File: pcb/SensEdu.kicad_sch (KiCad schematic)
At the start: 26 parts, among them J1 Power, J10 Barrel_Jack_Switch, J13 Conn_02x01, J14 Conn_02x01, J15 Conn_02x01, J2 PWM, J3 Analog, J4 PWM, J5 Analog, J6 Communication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

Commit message: Polishin pt1
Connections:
- net 5V0: now reaches J1.5 (Pin_5), JP3.3 (B)
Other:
- company: Infineon -> Infineon Technologies
- title: ArduinoGIGAR1_MicrophoneSpeakerBoard_SENSEDU_V1 -> SensEdu 0.7
- moved on the sheet: C3, C36, C37, C38, C4, C55, C56, C57, D1, FB1, FB2, J1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

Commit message: feat: Polished Sensedu schematics
Renamed Sheets
Added Nets
Repaired connections
Renamed Datasheets
Generated new schematic PDF
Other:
- sheet DPS310 renamed Pressure Sensor
- note added: "* PWM PINS"
- note added: "ARDUINO CONNECTORS"
- note added: "POWER"
- note removed: "* Indicates a PWM-capable pin"
- moved on the sheet: C3, C36, C37, C38, C4, C55, C56, C57, D1, FB1, FB2, J10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

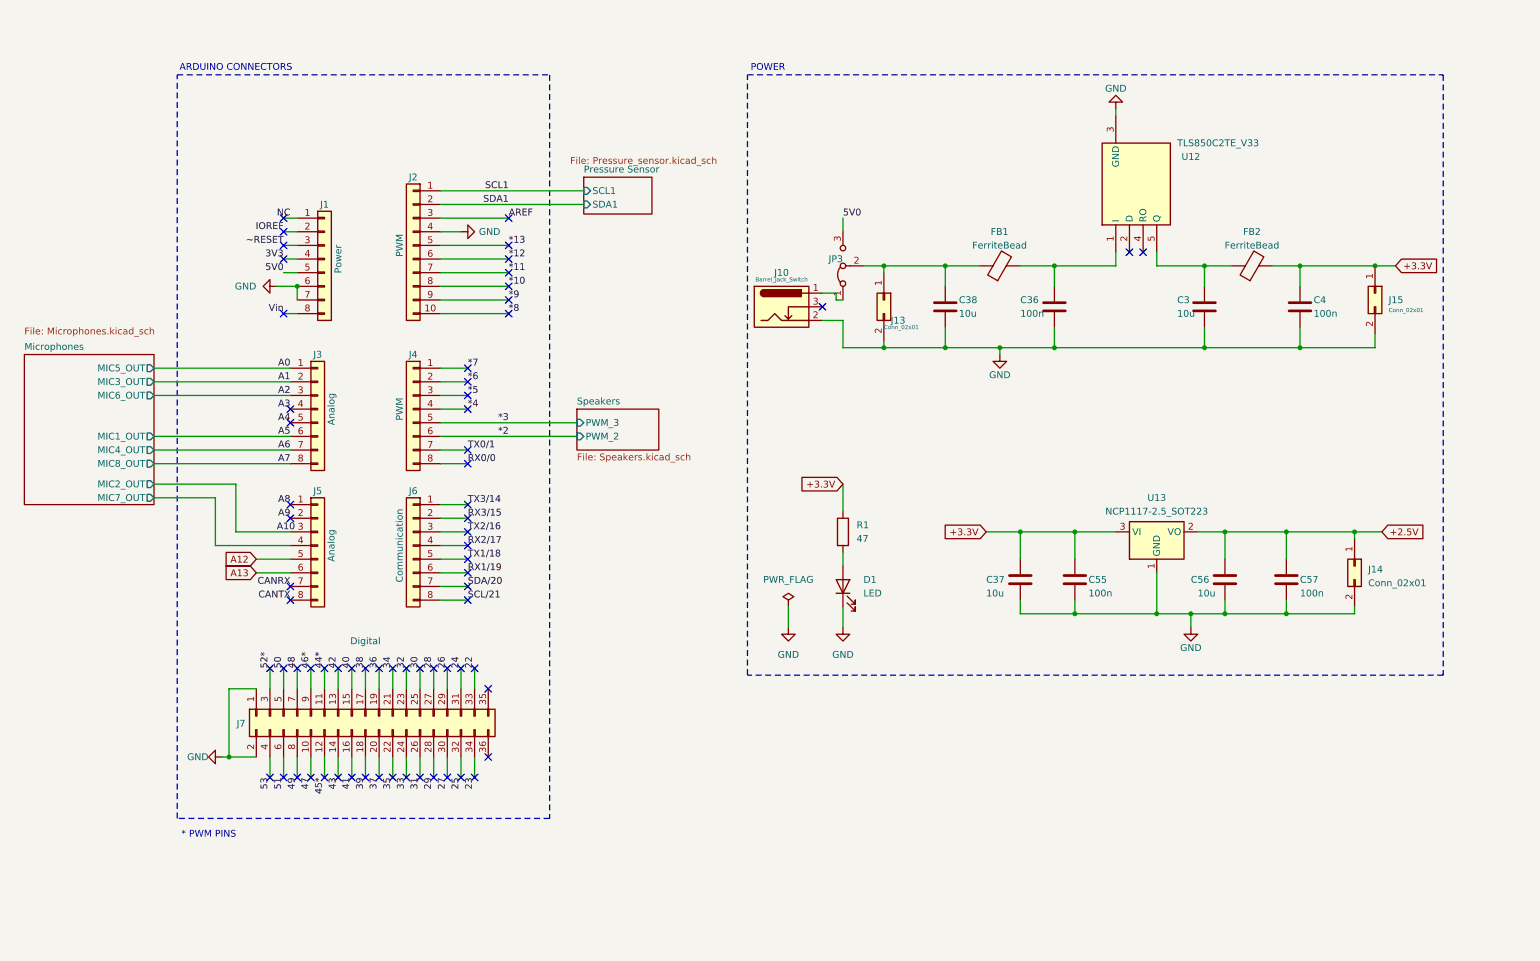
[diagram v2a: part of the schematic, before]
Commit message: refactor: Edit speaker/mic symbols and polish
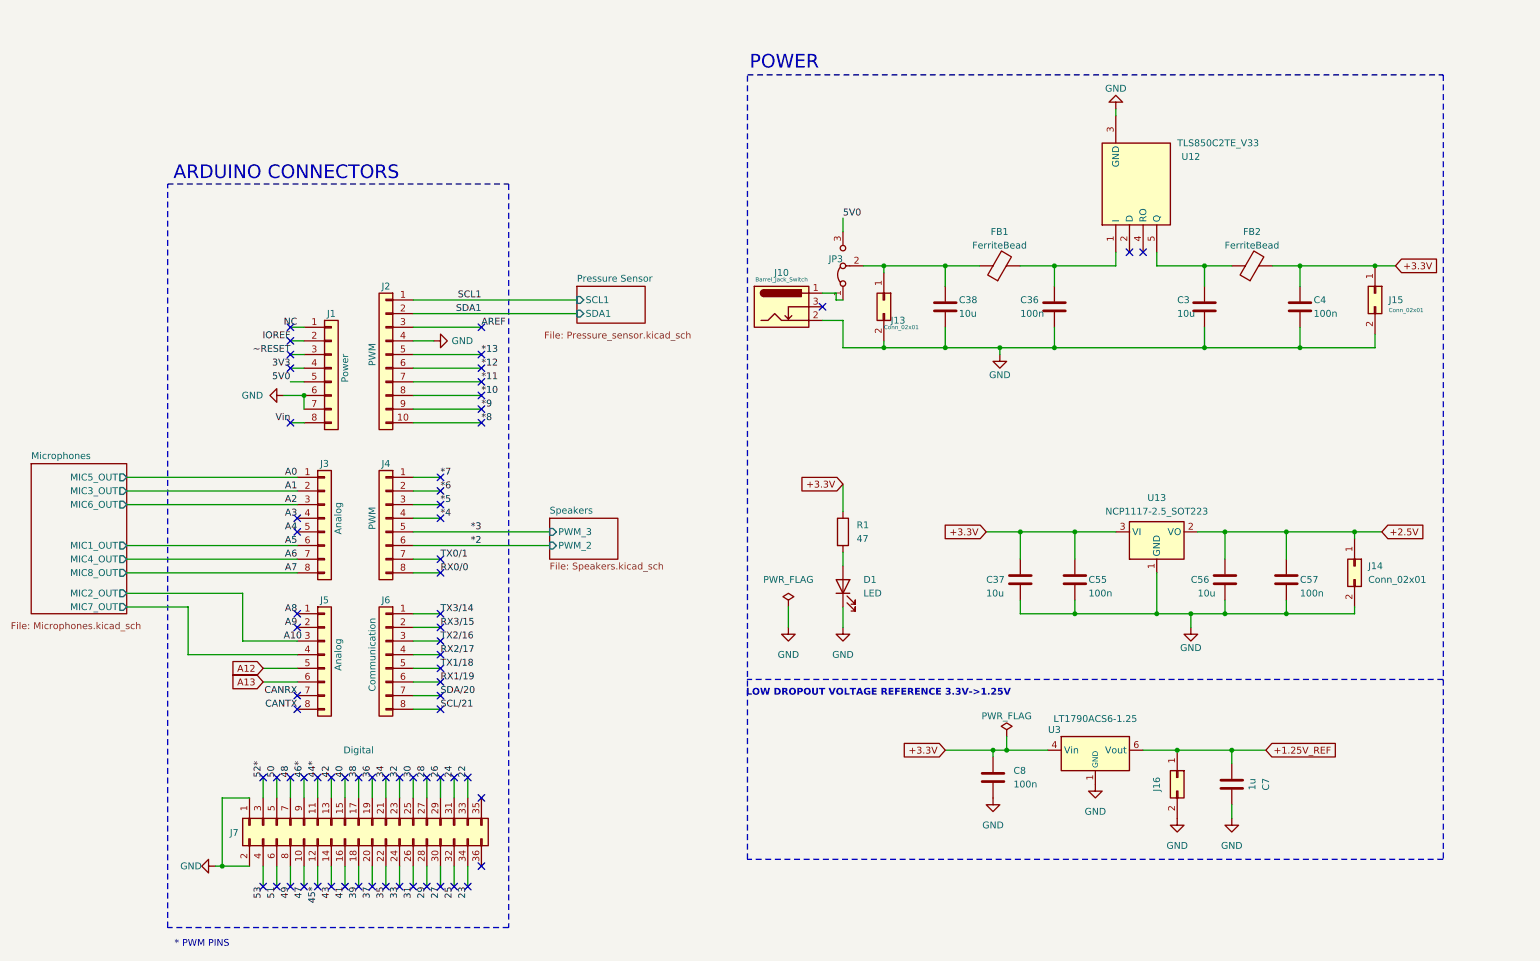
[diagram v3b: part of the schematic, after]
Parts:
- added C7: 1u, Capacitor_SMD:C_0805_2012Metric, symbol Device:C
- added C8: 100n, Capacitor_SMD:C_0805_2012Metric, symbol Device:C
- added J16: Conn_02x01, Connector_PinSocket_2.54mm:PinSocket_1x02_P2.54mm_Vertical, symbol Connector_Generic:Conn_02x01
- added U3: LT1790ACS6-1.25, Package_TO_SOT_SMD:TSOT-23-6, symbol SensEdu:LT1790-2.5_sensedu
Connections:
- net +3.3V: now also C8.1, U3.4 (Vin)
- net GND: now also C7.1, C8.2, J16.2 (Pin_2), U3.1 (GND), U3.2 (GND)
- new net +1.25V_REF: C7.2, J16.1 (Pin_1), U3.6 (Vout)
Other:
- note added: "LOW DROPOUT VOLTAGE REFERENCE 3.3V->1.25V"
- moved on the sheet: J1, J2, J3, J4, J5, J6, J7
